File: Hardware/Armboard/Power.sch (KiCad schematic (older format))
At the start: 13 parts, among them J1 Test_Point, U1 LM2576D2TR4

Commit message: Added more footprints
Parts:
- 47uF1, 47uF2: footprint (none) -> Capacitor_SMD:CP_Elec_5x5.4
- D8: footprint (none) -> Diode_SMD:D_SOD-323_HandSoldering
- J1: footprint (none) -> TestPoint:TestPoint_Pad_D2.5mm
- U1: footprint (none) -> MRDT_Devices:LM2576
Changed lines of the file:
@@
 F 0 "47uF1" H 8720 4156 50  0000 L CNN
 F 1 "CP1" H 8720 4065 50  0000 L CNN
-F 2 "" H 8605 4110 50  0001 C CNN
+F 2 "Capacitor_SMD:CP_Elec_5x5.4" H 8605 4110 50  0001 C CNN
 F 3 "~" H 8605 4110 50  0001 C CNN
 	1    8605 4110
@@
 F 0 "47uF2" H 9120 4156 50  0000 L CNN
 F 1 "CP2" H 9120 4065 50  0000 L CNN
-F 2 "" H 9005 4110 50  0001 C CNN
+F 2 "Capacitor_SMD:CP_Elec_5x5.4" H 9005 4110 50  0001 C CNN
 F 3 "~" H 9005 4110 50  0001 C CNN
 	1    9005 4110
@@
 F 0 "U1" H 2670 4745 50  0000 C CNN
 F 1 "LM2576D2TR4" H 2670 4654 50  0000 C CNN
-F 2 "" H 2670 4770 50  0001 C CNN
+F 2 "MRDT_Devices:LM2576" H 2670 4770 50  0001 C CNN
 F 3 "https://www.mouser.com/datasheet/2/308/LM2576_D-1810688.pdf" H 2670 4770 50  0001 C CNN
 	1    2670 4320
@@
 F 0 "J1" H 5042 4409 60  0000 R CNN
 F 1 "Test_Point" H 5042 4515 60  0000 R CNN
-F 2 "" H 5120 4320 60  0001 C CNN
+F 2 "TestPoint:TestPoint_Pad_D2.5mm" H 5120 4320 60  0001 C CNN
 F 3 "" H 5120 4320 60  0001 C CNN
 	1    5120 4370
@@
 F 0 "D8" V 3616 4340 50  0000 R CNN
 F 1 "D_Schottky" V 3525 4340 50  0000 R CNN
-F 2 "" H 3570 4420 50  0001 C CNN
+F 2 "Diode_SMD:D_SOD-323_HandSoldering" H 3570 4420 50  0001 C CNN
 F 3 "~" H 3570 4420 50  0001 C CNN
 	1    3570 4420

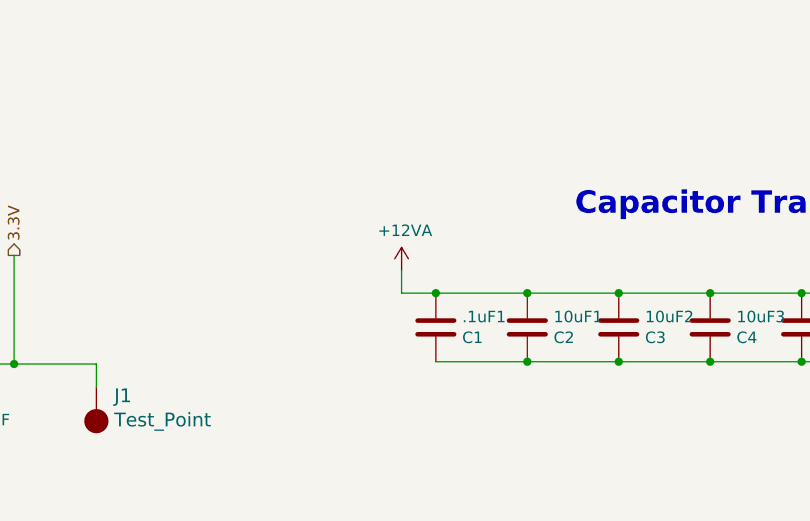
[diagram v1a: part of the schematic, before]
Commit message: Fixed Andersons, made netlist, imported footprints to layout
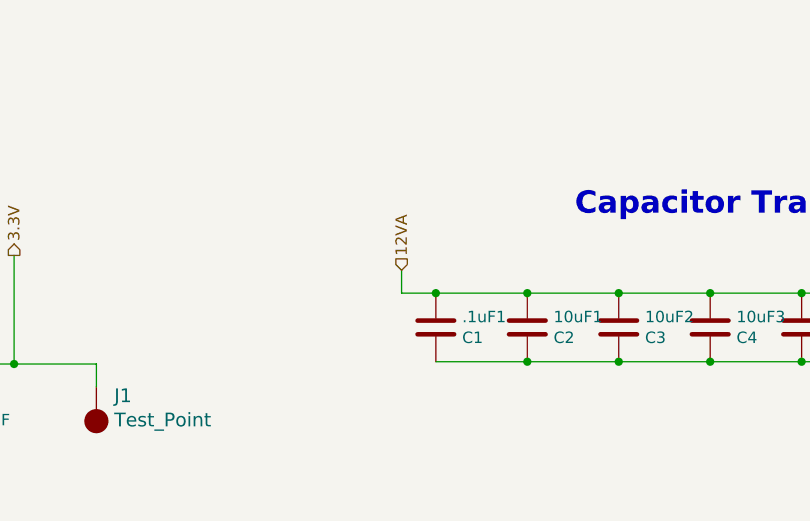
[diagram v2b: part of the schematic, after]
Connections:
- net +12VA renamed 12VA
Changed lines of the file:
@@
-$EndComp
-$Comp
-L power:+12VA #PWR012
-U 1 1 5F680B53
-P 6455 3860
-F 0 "#PWR012" H 6455 3710 50  0001 C CNN
-F 1 "+12VA" H 6470 4033 50  0000 C CNN
-F 2 "" H 6455 3860 50  0001 C CNN
-F 3 "" H 6455 3860 50  0001 C CNN
-	1    6455 3860
-	1    0    0    -1
 $EndComp
 $Comp
@@
 Wire Wire Line
 	4760 4270 5120 4270
+Text HLabel 6455 3860 1    50   Input ~ 0
+12VA
 $EndSCHEMATC

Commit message: Finished general component layout
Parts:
- D8: footprint Diode_SMD:D_SOD-323_HandSoldering -> Diode_THT:D_DO-201AD_P15.24mm_Horizontal
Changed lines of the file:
@@
 F 0 "D8" V 3616 4340 50  0000 R CNN
 F 1 "D_Schottky" V 3525 4340 50  0000 R CNN
-F 2 "Diode_SMD:D_SOD-323_HandSoldering" H 3570 4420 50  0001 C CNN
+F 2 "Diode_THT:D_DO-201AD_P15.24mm_Horizontal" H 3570 4420 50  0001 C CNN
 F 3 "~" H 3570 4420 50  0001 C CNN
 	1    3570 4420

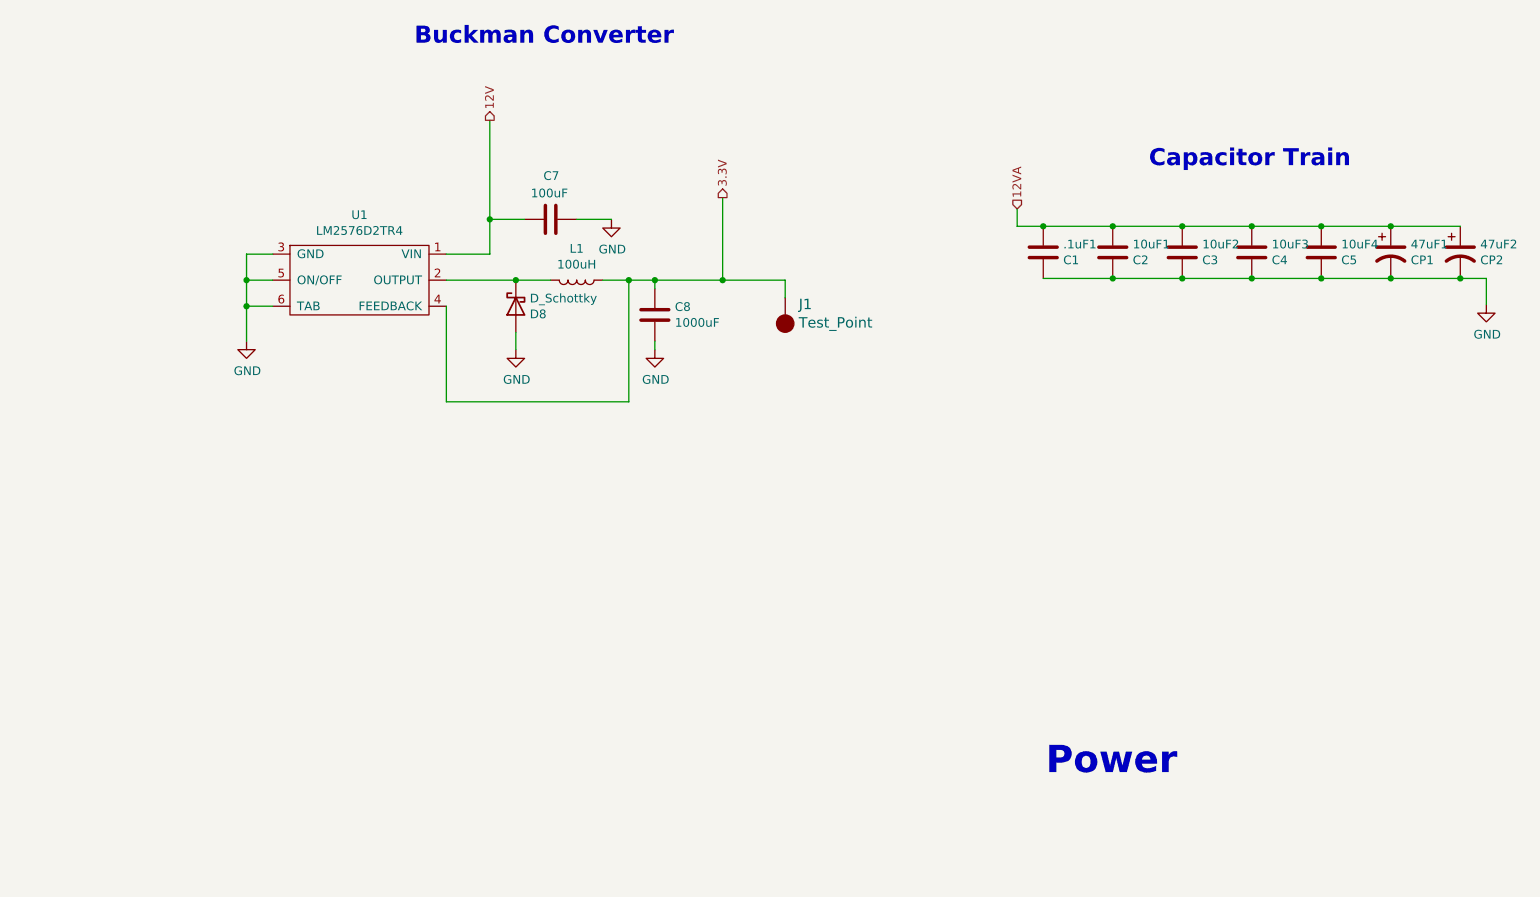
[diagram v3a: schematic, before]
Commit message: Double-checked schematic, pointed power pins up, made sure 12V and 3.3V were full networks
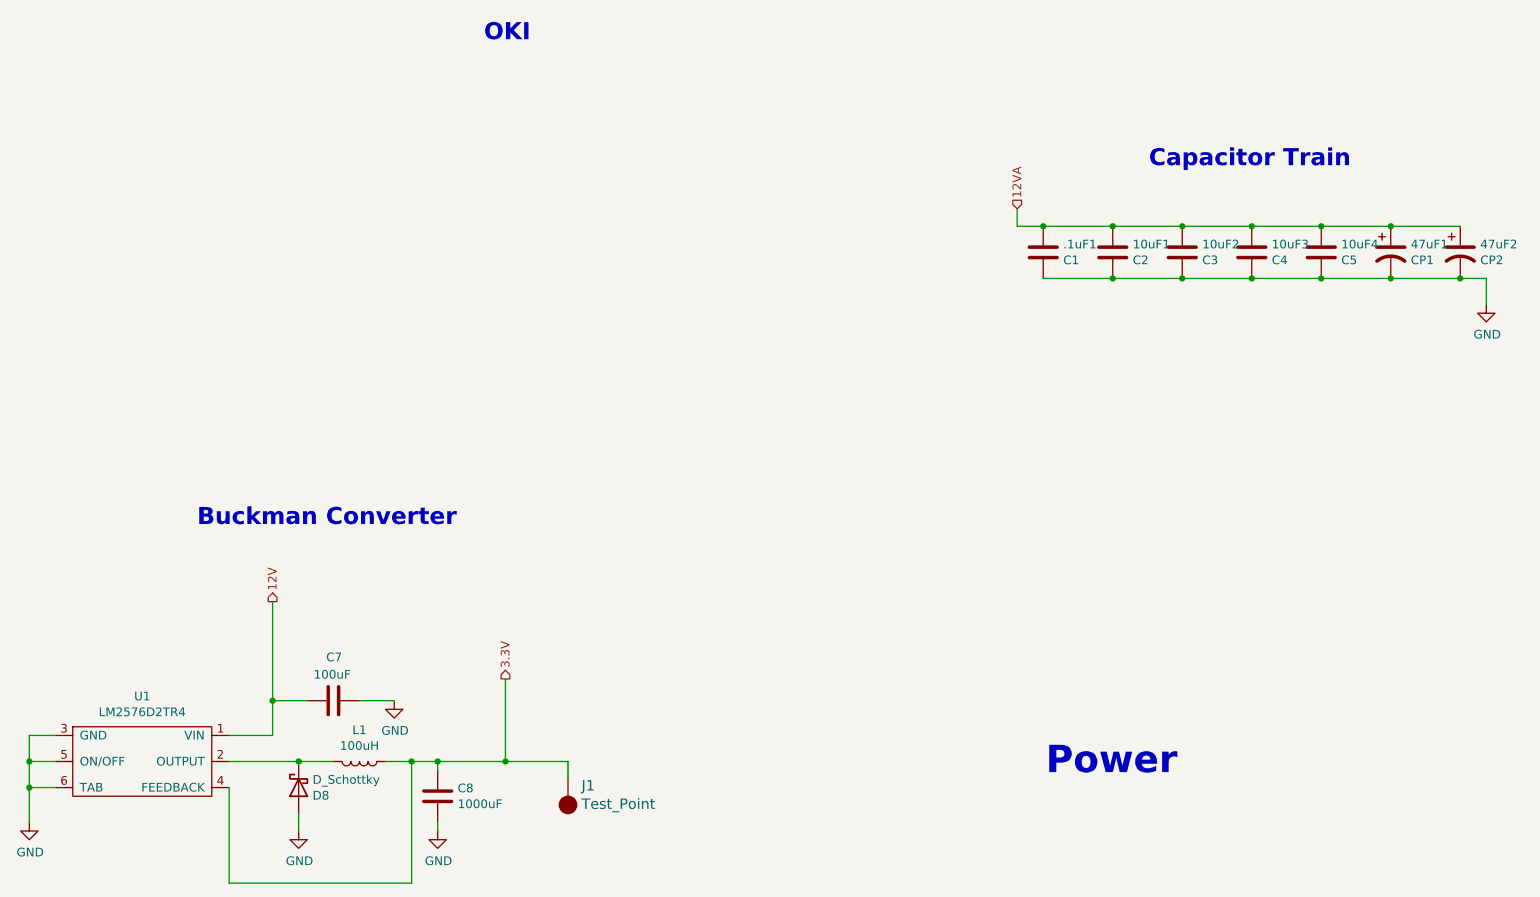
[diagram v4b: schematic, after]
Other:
- note added: "OKI"
- moved on the sheet: C7, C8, D8, J1, L1, U1
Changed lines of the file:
@@
 L Armboard-rescue:LM2576D2TR4-MRDT_Devices-Armboard-rescue U1
 U 1 1 5F74DE4A
-P 2670 4320
-F 0 "U1" H 2670 4745 50  0000 C CNN
-F 1 "LM2576D2TR4" H 2670 4654 50  0000 C CNN
-F 2 "MRDT_Devices:LM2576" H 2670 4770 50  0001 C CNN
-F 3 "https://www.mouser.com/datasheet/2/308/LM2576_D-1810688.pdf" H 2670 4770 50  0001 C CNN
-	1    2670 4320
+P 1420 7090
+F 0 "U1" H 1420 7515 50  0000 C CNN
+F 1 "LM2576D2TR4" H 1420 7424 50  0000 C CNN
+F 2 "MRDT_Devices:LM2576" H 1420 7540 50  0001 C CNN
+F 3 "https://www.mouser.com/datasheet/2/308/LM2576_D-1810688.pdf" H 1420 7540 50  0001 C CNN
+	1    1420 7090
 	1    0    0    -1
 $EndComp
@@
 L power:GND #PWR08
 U 1 1 5F74E2A1
-P 2020 4620
-F 0 "#PWR08" H 2020 4370 50  0001 C CNN
-F 1 "GND" H 2025 4447 50  0000 C CNN
-F 2 "" H 2020 4620 50  0001 C CNN
-F 3 "" H 2020 4620 50  0001 C CNN
-	1    2020 4620
+P 770 7390
+F 0 "#PWR08" H 770 7140 50  0001 C CNN
+F 1 "GND" H 775 7217 50  0000 C CNN
+F 2 "" H 770 7390 50  0001 C CNN
+F 3 "" H 770 7390 50  0001 C CNN
+	1    770  7390
 	1    0    0    -1
 $EndComp
 Wire Wire Line
-	2170 4120 2020 4120
+	920  6890 770  6890
 Wire Wire Line
-	2170 4270 2020 4270
+	920  7040 770  7040
 Wire Wire Line
-	2020 4120 2020 4270
-Connection ~ 2020 4270
+	770  6890 770  7040
+Connection ~ 770  7040
 Wire Wire Line
-	2170 4420 2020 4420
+	920  7190 770  7190
 Wire Wire Line
-	2020 4270 2020 4420
-Connection ~ 2020 4420
+	770  7040 770  7190
+Connection ~ 770  7190
 Wire Wire Line
-	2020 4420 2020 4620
+	770  7190 770  7390
 Wire Wire Line
-	3170 4120 3420 4120
+	1920 6890 2170 6890
 Wire Wire Line
-	3420 4120 3420 3920
+	2170 6890 2170 6690
 $Comp
 L Device:C C8
 U 1 1 5F750C41
-P 4370 4470
-F 0 "C8" H 4485 4516 50  0000 L CNN
-F 1 "1000uF" H 4485 4425 50  0000 L CNN
-F 2 "Capacitor_SMD:C_0603_1608Metric_Pad1.05x0.95mm_HandSolder" H 4408 4320 50  0001 C CNN
-F 3 "~" H 4370 4470 50  0001 C CNN
-	1    4370 4470
+P 3120 7240
+F 0 "C8" H 3235 7286 50  0000 L CNN
+F 1 "1000uF" H 3235 7195 50  0000 L CNN
+F 2 "Capacitor_SMD:C_0603_1608Metric_Pad1.05x0.95mm_HandSolder" H 3158 7090 50  0001 C CNN
+F 3 "~" H 3120 7240 50  0001 C CNN
+	1    3120 7240
 	1    0    0    -1
 $EndComp
@@
 L Device:C C7
 U 1 1 5F75145E
-P 3770 3920
-F 0 "C7" V 4020 3870 50  0000 L CNN
-F 1 "100uF" V 3920 3820 50  0000 L CNN
-F 2 "Capacitor_SMD:C_0603_1608Metric_Pad1.05x0.95mm_HandSolder" H 3808 3770 50  0001 C CNN
-F 3 "~" H 3770 3920 50  0001 C CNN
-	1    3770 3920
+P 2520 6690
+F 0 "C7" V 2770 6640 50  0000 L CNN
+F 1 "100uF" V 2670 6590 50  0000 L CNN
+F 2 "Capacitor_SMD:C_0603_1608Metric_Pad1.05x0.95mm_HandSolder" H 2558 6540 50  0001 C CNN
+F 3 "~" H 2520 6690 50  0001 C CNN
+	1    2520 6690
 	0    -1   -1   0
 $EndComp
 Wire Wire Line
-	3420 3920 3620 3920
-Connection ~ 3420 3920
+	2170 6690 2370 6690
+Connection ~ 2170 6690
 $Comp
 L power:GND #PWR010
 U 1 1 5F75423C
-P 4120 3920
-F 0 "#PWR010" H 4120 3670 50  0001 C CNN
-F 1 "GND" H 4125 3747 50  0000 C CNN
-F 2 "" H 4120 3920 50  0001 C CNN
-F 3 "" H 4120 3920 50  0001 C CNN
-	1    4120 3920
+P 2870 6690
+F 0 "#PWR010" H 2870 6440 50  0001 C CNN
+F 1 "GND" H 2875 6517 50  0000 C CNN
+F 2 "" H 2870 6690 50  0001 C CNN
+F 3 "" H 2870 6690 50  0001 C CNN
+	1    2870 6690
 	1    0    0    -1
 $EndComp
 Wire Wire Line
-	3920 3920 4120 3920
+	2670 6690 2870 6690
 $Comp
 L Device:L L1
 U 1 1 5F755388
-P 3920 4270
-F 0 "L1" V 3739 4270 50  0000 C CNN
-F 1 "100uH" V 3830 4270 50  0000 C CNN
-F 2 "Inductor_SMD:L_0603_1608Metric_Pad1.05x0.95mm_HandSolder" H 3920 4270 50  0001 C CNN
-F 3 "~" H 3920 4270 50  0001 C CNN
-	1    3920 4270
+P 2670 7040
+F 0 "L1" V 2489 7040 50  0000 C CNN
+F 1 "100uH" V 2580 7040 50  0000 C CNN
+F 2 "Inductor_SMD:L_0603_1608Metric_Pad1.05x0.95mm_HandSolder" H 2670 7040 50  0001 C CNN
+F 3 "~" H 2670 7040 50  0001 C CNN
+	1    2670 7040
 	0    1    1    0
 $EndComp
@@
 L power:GND #PWR09
 U 1 1 5F75782E
-P 3570 4670
-F 0 "#PWR09" H 3570 4420 50  0001 C CNN
-F 1 "GND" H 3575 4497 50  0000 C CNN
-F 2 "" H 3570 4670 50  0001 C CNN
-F 3 "" H 3570 4670 50  0001 C CNN
-	1    3570 4670
+P 2320 7440
+F 0 "#PWR09" H 2320 7190 50  0001 C CNN
+F 1 "GND" H 2325 7267 50  0000 C CNN
+F 2 "" H 2320 7440 50  0001 C CNN
+F 3 "" H 2320 7440 50  0001 C CNN
+	1    2320 7440
 	1    0    0    -1
 $EndComp
 Wire Wire Line
-	3570 4570 3570 4670
+	2320 7340 2320 7440
 Wire Wire Line
-	4070 4270 4220 4270
+	2820 7040 2970 7040
 Wire Wire Line
-	4370 4270 4370 4320
+	3120 7040 3120 7090
 Wire Wire Line
-	3170 4420 3170 4970
+	1920 7190 1920 7740
 Wire Wire Line
-	3170 4970 4220 4970
+	1920 7740 2970 7740
 Wire Wire Line
-	4220 4970 4220 4270
-Connection ~ 4220 4270
+	2970 7740 2970 7040
+Connection ~ 2970 7040
 Wire Wire Line
-	4220 4270 4370 4270
+	2970 7040 3120 7040
 $Comp
 L power:GND #PWR011
 U 1 1 5F75A24F
-P 4370 4670
-F 0 "#PWR011" H 4370 4420 50  0001 C CNN
-F 1 "GND" H 4375 4497 50  0000 C CNN
-F 2 "" H 4370 4670 50  0001 C CNN
-F 3 "" H 4370 4670 50  0001 C CNN
-	1    4370 4670
+P 3120 7440
+F 0 "#PWR011" H 3120 7190 50  0001 C CNN
+F 1 "GND" H 3125 7267 50  0000 C CNN
+F 2 "" H 3120 7440 50  0001 C CNN
+F 3 "" H 3120 7440 50  0001 C CNN
+	1    3120 7440
 	1    0    0    -1
 $EndComp
 Wire Wire Line
-	4370 4670 4370 4620
+	3120 7440 3120 7390
 $Comp
 L Armboard-rescue:Test_Point-MRDT_Connectors-Armboard-rescue J1
 U 1 1 5F75C39D
-P 5120 4370
-F 0 "J1" H 5042 4409 60  0000 R CNN
-F 1 "Test_Point" H 5042 4515 60  0000 R CNN
-F 2 "TestPoint:TestPoint_Pad_D2.5mm" H 5120 4320 60  0001 C CNN
-F 3 "" H 5120 4320 60  0001 C CNN
-	1    5120 4370
+P 3870 7140
+F 0 "J1" H 3792 7179 60  0000 R CNN
+F 1 "Test_Point" H 3792 7285 60  0000 R CNN
+F 2 "TestPoint:TestPoint_Pad_D2.5mm" H 3870 7090 60  0001 C CNN
+F 3 "" H 3870 7090 60  0001 C CNN
+	1    3870 7140
 	-1   0    0    1
 $EndComp
 Wire Wire Line
-	5120 4270 5120 4370
-Connection ~ 4370 4270
-Text Notes 4480 2925 2    98   ~ 20
+	3870 7040 3870 7140
+Connection ~ 3120 7040
+Text Notes 3230 5695 2    98   ~ 20
 Buckman Converter
 Text Notes 8375 3630 2    98   ~ 20
@@
 L Device:D_Schottky D8
 U 1 1 5F83C9A2
-P 3570 4420
-F 0 "D8" V 3616 4340 50  0000 R CNN
-F 1 "D_Schottky" V 3525 4340 50  0000 R CNN
-F 2 "Diode_THT:D_DO-201AD_P15.24mm_Horizontal" H 3570 4420 50  0001 C CNN
-F 3 "~" H 3570 4420 50  0001 C CNN
-	1    3570 4420
+P 2320 7190
+F 0 "D8" V 2366 7110 50  0000 R CNN
+F 1 "D_Schottky" V 2275 7110 50  0000 R CNN
+F 2 "Diode_THT:D_DO-201AD_P15.24mm_Horizontal" H 2320 7190 50  0001 C CNN
+F 3 "~" H 2320 7190 50  0001 C CNN
+	1    2320 7190
 	0    -1   1    0
 $EndComp
 Wire Wire Line
-	3170 4270 3570 4270
-Connection ~ 3570 4270
+	1920 7040 2320 7040
+Connection ~ 2320 7040
 Wire Wire Line
-	3570 4270 3770 4270
+	2320 7040 2520 7040
 Text Notes 6620 7130 0    157  ~ 31
 Power
-Text HLabel 4760 3795 1    50   Output ~ 0
+Text HLabel 3510 6565 1    50   Output ~ 0
 3.3V
-Text HLabel 3420 3350 1    50   Output ~ 0
+Text HLabel 2170 6120 1    50   Output ~ 0
 12V
 Wire Wire Line
-	3420 3350 3420 3920
+	2170 6120 2170 6690
 Wire Wire Line
-	4370 4270 4760 4270
+	3120 7040 3510 7040
 Wire Wire Line
-	4760 3795 4760 4270
-Connection ~ 4760 4270
+	3510 6565 3510 7040
+Connection ~ 3510 7040
 Wire Wire Line
-	4760 4270 5120 4270
+	3510 7040 3870 7040
 Text HLabel 6455 3860 1    50   Input ~ 0
 12VA
+Text Notes 3655 2905 2    98   ~ 20
+OKI
 $EndSCHEMATC
